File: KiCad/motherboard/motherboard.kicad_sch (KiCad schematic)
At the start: 558 parts, among them J1 Conn_01x06_Pin, J10 Conn_01x04_Pin, J11 DB25_Socket_MountingHoles, J12 Conn_01x04_Pin, J13 1761681-9, J14 Conn_01x04_Pin, J15 1761681-9, J2 Barrel_Jack_Switch, J3 Conn_01x04_Pin, J4 Conn_01x05_Pin, J5 Conn_01x06_Pin, J6 Conn_01x04_Pin, J7 Conn_01x09_Pin, J8 Conn_01x02_Socket, J9 Conn_01x04_Pin, Q1 BSS138, Q2 BSS138, Q3 SI2369DS-T1-GE3, Q4 BSS138, Q5 BSS138, Q6 BSS138, Q7 BSS138, SW1 EmergencyStop, SW2 TiltSwitch, SW3 DoorSwitch, SW4 AdditionalSlot, SW5 SW_Push, SW6 SW_Push, SW7 SW_Push, SW8 SW_Push, U1 P7803B-1000, U10 24LC512, U2 P7805B-1000, U4 ASSR-1218, U5 TMC2209, U6 TMC2209, U8 LTV-817S, U9 LTV-817S

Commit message: PPT
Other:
- title: (none) -> Motherboard
- moved on the sheet: JP100, JP101, JP102, JP103, JP104, JP121, JP122, JP123, JP124, JP125, JP126, JP127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

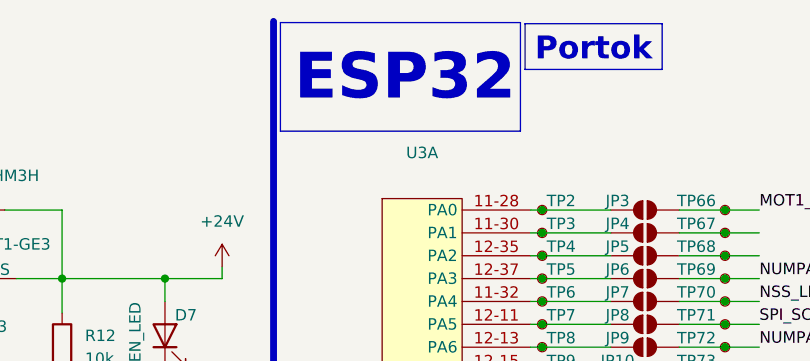
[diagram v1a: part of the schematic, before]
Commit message: PCB bugfixes based on review
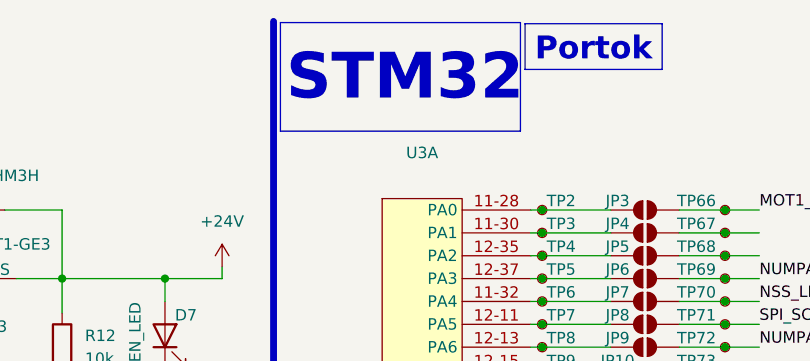
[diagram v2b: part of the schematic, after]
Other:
- note added: "STM32"
- note removed: "ESP32"
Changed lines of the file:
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@@
 		)
 	)
-	(text "ESP32"
+	(text "STM32"
 		(exclude_from_sim no)
 		(at 137.16 18.415 0)

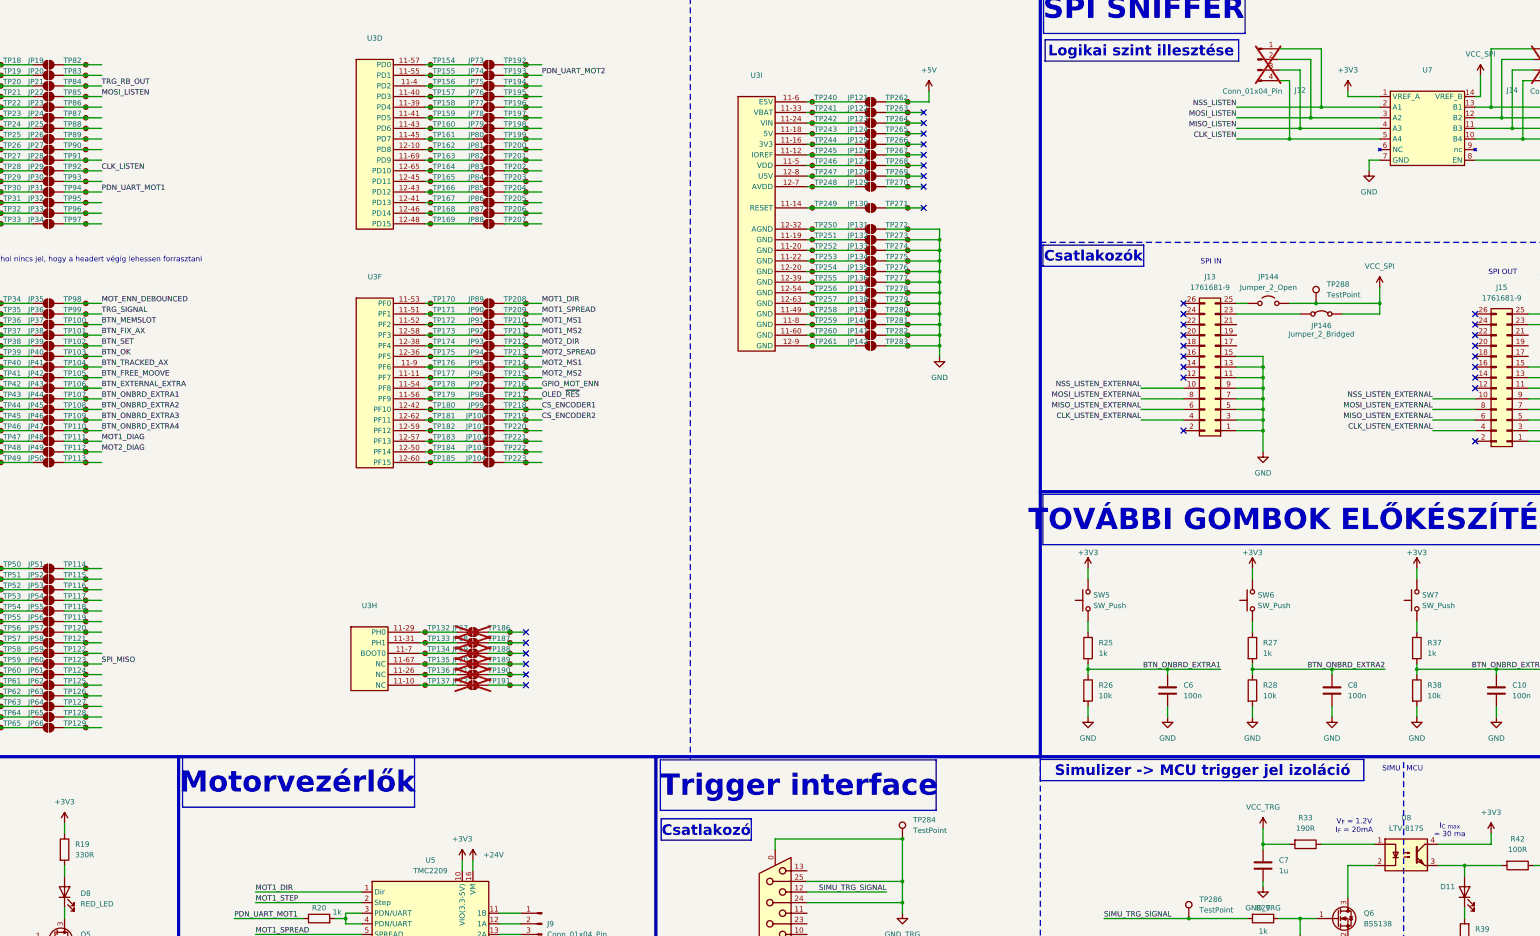
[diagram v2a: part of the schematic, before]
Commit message: documentation, OLED demo, BOM
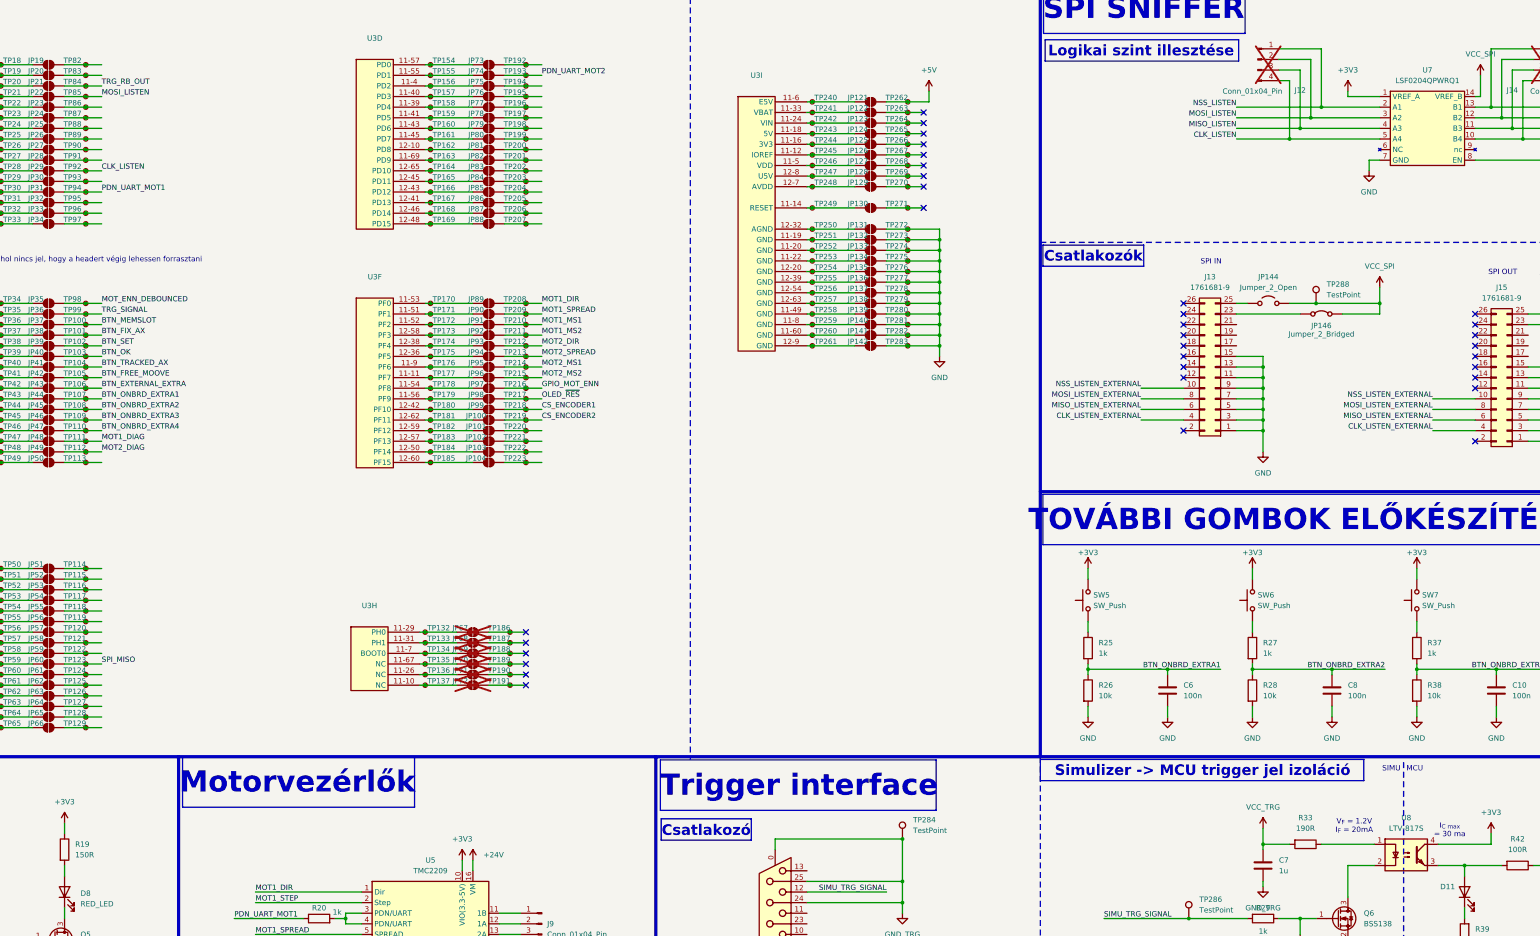
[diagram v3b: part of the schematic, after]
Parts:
- J13, J15: footprint Connector_PinHeader_2.54mm:PinHeader_2x13_P2.54mm_Vertical -> Connector_IDC:IDC-Header_2x13_P2.54mm_Vertical
- R19: value 330R -> 150R
- U7: value ~ -> LSF0204QPWRQ1
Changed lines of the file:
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@@
 			)
 		)
-		(property "Footprint" "Connector_PinHeader_2.54mm:PinHeader_2x13_P2.54mm_Vertical"
+		(property "Footprint" "Connector_IDC:IDC-Header_2x13_P2.54mm_Vertical"
 			(at 513.08 165.1 0)
 			(effects
@@
 			)
 		)
-		(property "Value" "330R"
+		(property "Value" "150R"
 			(at 170.18 279.3999 0)
 			(effects
@@
 			)
 		)
-		(property "Value" "~"
+		(property "Value" "LSF0204QPWRQ1"
 			(at 494.03 93.98 0)
 			(effects
@@
 			)
 		)
-		(property "Footprint" "Connector_PinHeader_2.54mm:PinHeader_2x13_P2.54mm_Vertical"
+		(property "Footprint" "Connector_IDC:IDC-Header_2x13_P2.54mm_Vertical"
 			(at 443.23 162.56 0)
 			(effects

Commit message: BOM
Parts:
- R33, R40: value 190R -> 150R
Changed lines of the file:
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@@
 			)
 		)
-		(property "Value" "190R"
+		(property "Value" "150R"
 			(at 464.82 273.05 90)
 			(effects
@@
 			)
 		)
-		(property "Value" "190R"
+		(property "Value" "150R"
 			(at 513.08 330.2 90)
 			(effects

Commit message: documentation and plots
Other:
- note added: "Visszajelző LED"
- note removed: "Visszajelző LEDek"
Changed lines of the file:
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@@
 		)
 	)
-	(text "Visszajelző LEDek"
+	(text "Visszajelző LED"
 		(exclude_from_sim no)
 		(at 127.635 259.08 0)
